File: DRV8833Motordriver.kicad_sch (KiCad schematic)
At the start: 8 parts, among them J1 Conn_01x06_Pin, J2 Conn_01x06_Pin, U1 DRV8833PWP

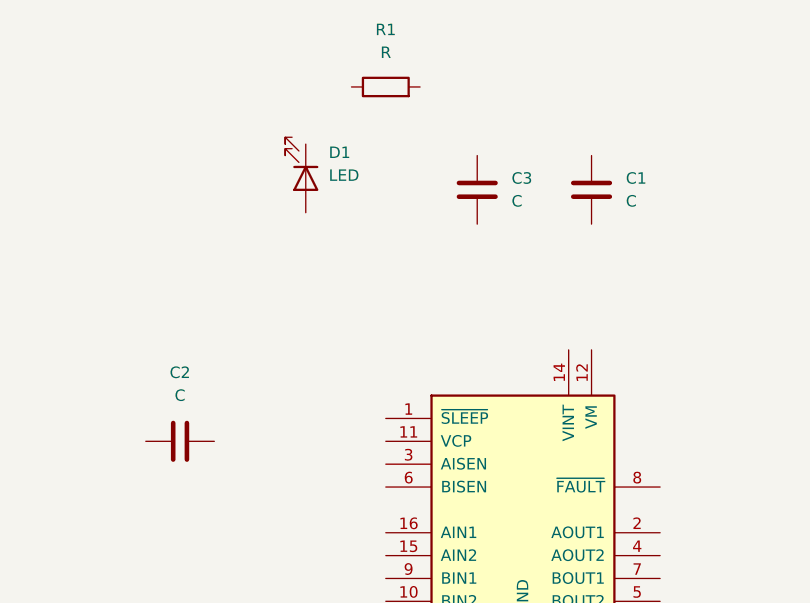
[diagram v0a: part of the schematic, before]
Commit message: Placed Normal Wires
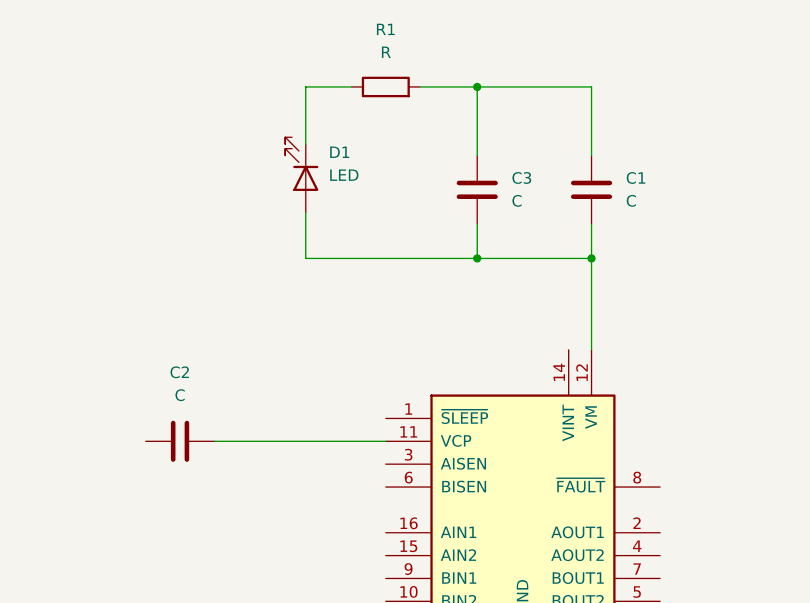
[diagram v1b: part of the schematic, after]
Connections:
- net at R1.1: now also D1.1 (K)
- net at R1.2: now also C1.1, C3.1
- net at C3.2: now also C1.2, D1.2 (A), U1.12 (VM)
- net at C2.2: now also U1.11 (VCP)
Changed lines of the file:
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@@
 	(generator_version "9.0")
 	(paper "A4")
+	(junction
+		(at 151.13 69.85)
+		(diameter 0)
+		(color 0 0 0 0)
+	)
+	(junction
+		(at 138.43 69.85)
+		(diameter 0)
+		(color 0 0 0 0)
+	)
+	(junction
+		(at 138.43 50.8)
+		(diameter 0)
+		(color 0 0 0 0)
+	)
+	(wire
+		(pts
+			(xy 119.38 50.8) (xy 124.46 50.8)
+		)
+		(stroke
+			(width 0)
+			(type default)
+		)
+	)
+	(wire
+		(pts
+			(xy 119.38 64.77) (xy 119.38 69.85)
+		)
+		(stroke
+			(width 0)
+			(type default)
+		)
+	)
+	(wire
+		(pts
+			(xy 138.43 69.85) (xy 151.13 69.85)
+		)
+		(stroke
+			(width 0)
+			(type default)
+		)
+	)
+	(wire
+		(pts
+			(xy 151.13 69.85) (xy 151.13 80.01)
+		)
+		(stroke
+			(width 0)
+			(type default)
+		)
+	)
+	(wire
+		(pts
+			(xy 138.43 66.04) (xy 138.43 69.85)
+		)
+		(stroke
+			(width 0)
+			(type default)
+		)
+	)
+	(wire
+		(pts
+			(xy 119.38 69.85) (xy 138.43 69.85)
+		)
+		(stroke
+			(width 0)
+			(type default)
+		)
+	)
+	(wire
+		(pts
+			(xy 138.43 50.8) (xy 132.08 50.8)
+		)
+		(stroke
+			(width 0)
+			(type default)
+		)
+	)
+	(wire
+		(pts
+			(xy 151.13 58.42) (xy 151.13 50.8)
+		)
+		(stroke
+			(width 0)
+			(type default)
+		)
+	)
+	(wire
+		(pts
+			(xy 151.13 66.04) (xy 151.13 69.85)
+		)
+		(stroke
+			(width 0)
+			(type default)
+		)
+	)
+	(wire
+		(pts
+			(xy 138.43 50.8) (xy 138.43 58.42)
+		)
+		(stroke
+			(width 0)
+			(type default)
+		)
+	)
+	(wire
+		(pts
+			(xy 109.22 90.17) (xy 128.27 90.17)
+		)
+		(stroke
+			(width 0)
+			(type default)
+		)
+	)
+	(wire
+		(pts
+			(xy 119.38 57.15) (xy 119.38 50.8)
+		)
+		(stroke
+			(width 0)
+			(type default)
+		)
+	)
+	(wire
+		(pts
+			(xy 151.13 50.8) (xy 138.43 50.8)
+		)
+		(stroke
+			(width 0)
+			(type default)
+		)
+	)
 	(symbol
 		(lib_id "Device:R")

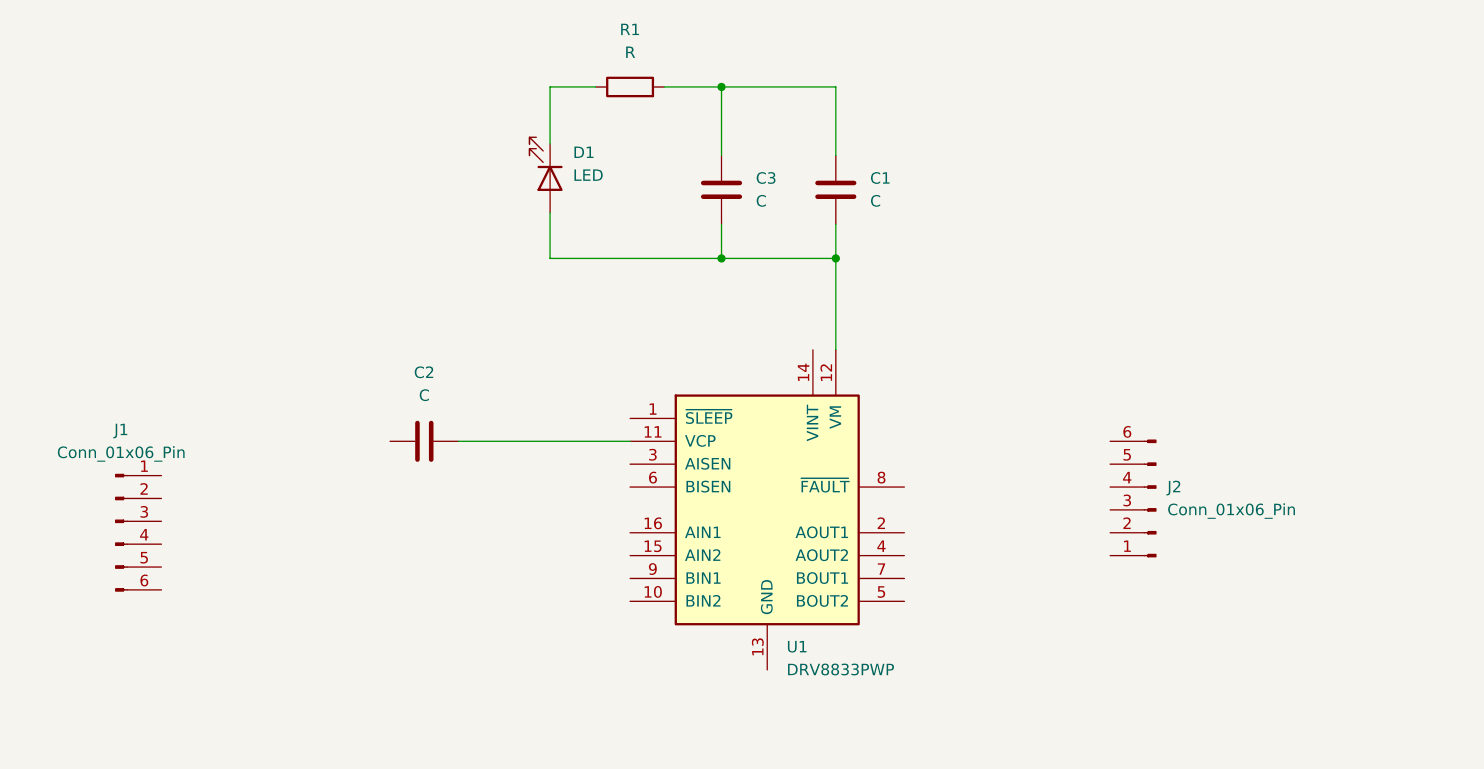
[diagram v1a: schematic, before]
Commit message: Added Net Labels to Wires
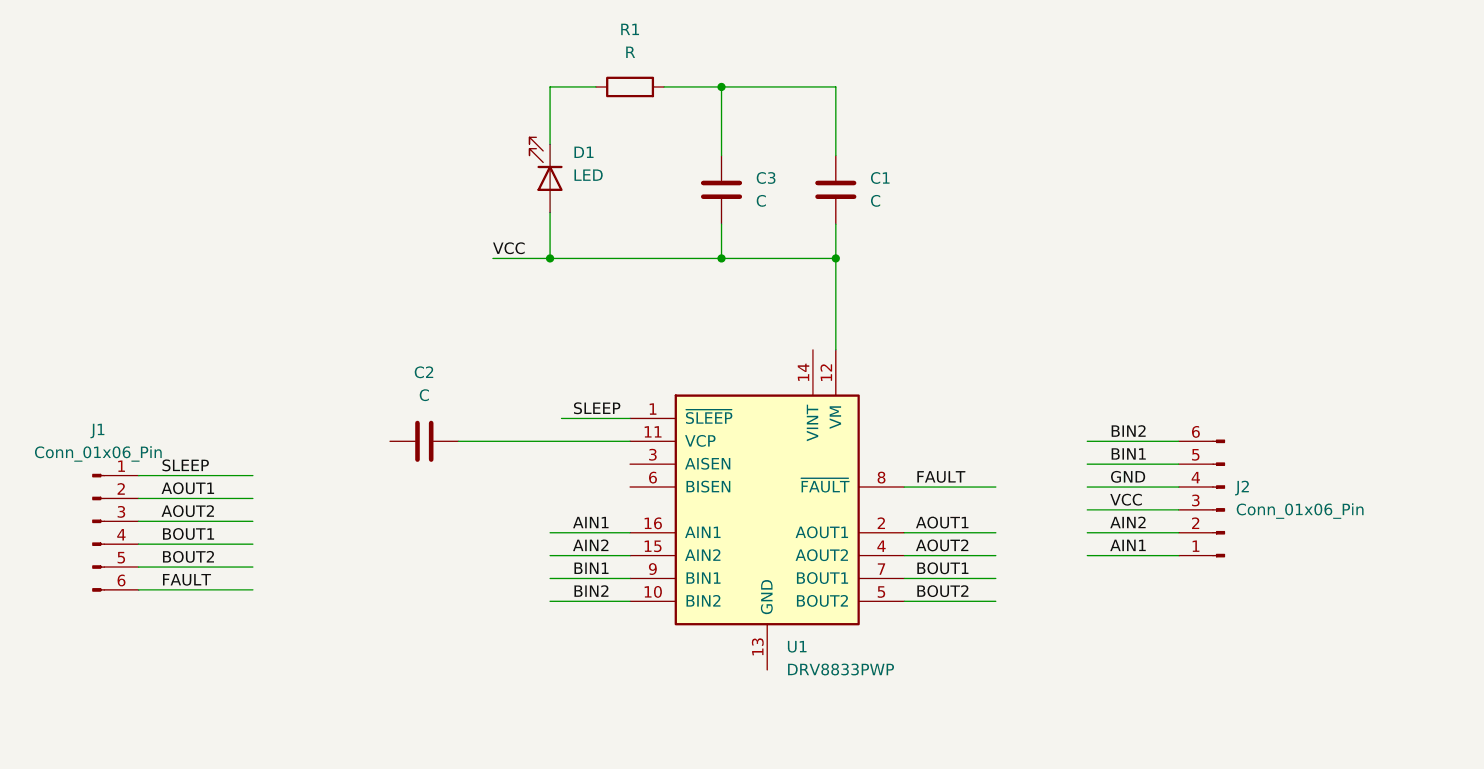
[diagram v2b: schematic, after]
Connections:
- net SLEEP: now reaches J1.1 (Pin_1)
- net SLEEP: now also U1.1 (~{SLEEP})
- net AOUT1: now reaches J1.2 (Pin_2)
- net AOUT1: now also U1.2 (AOUT1)
- net AOUT2: now reaches J1.3 (Pin_3)
- net AOUT2: now also U1.4 (AOUT2)
- net BOUT1: now reaches J1.4 (Pin_4)
- net BOUT1: now also U1.7 (BOUT1)
- net BOUT2: now reaches J1.5 (Pin_5)
- net BOUT2: now also U1.5 (BOUT2)
- net FAULT: now reaches J1.6 (Pin_6)
- net FAULT: now also U1.8 (~{FAULT})
- net VCC: now reaches C1.2, C3.2, D1.2 (A), U1.12 (VM)
- net VCC: now also J2.3 (Pin_3)
- net BIN2: now reaches U1.10 (BIN2)
- net BIN2: now also J2.6 (Pin_6)
- net AIN2: now reaches U1.15 (AIN2)
- net AIN2: now also J2.2 (Pin_2)
- net AIN1: now reaches U1.16 (AIN1)
- net AIN1: now also J2.1 (Pin_1)
- net BIN1: now reaches U1.9 (BIN1)
- net BIN1: now also J2.5 (Pin_5)
- net GND: now reaches J2.4 (Pin_4)
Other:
- moved on the sheet: J1, J2

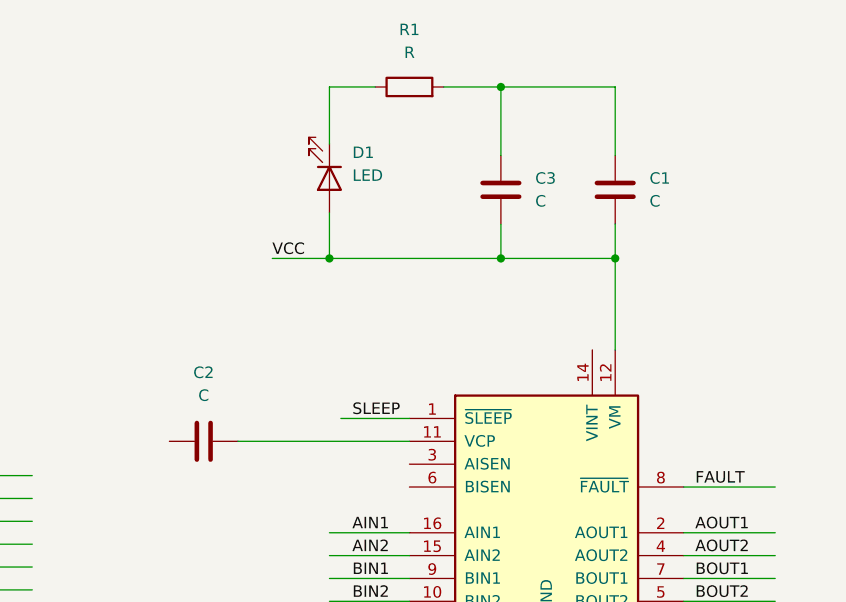
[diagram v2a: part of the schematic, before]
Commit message: Added Values to Components
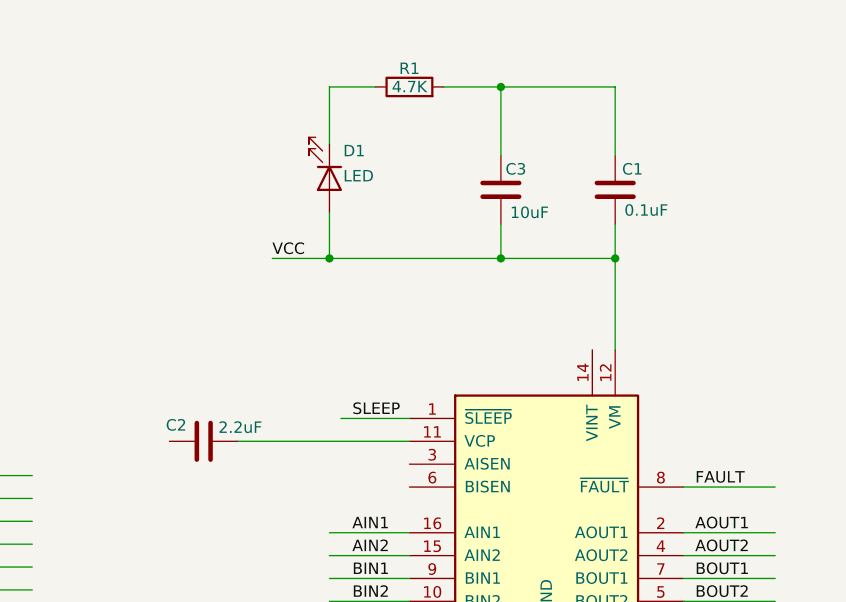
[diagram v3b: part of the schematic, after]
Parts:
- C1: value C -> 0.1uF
- C2: value C -> 2.2uF
- C3: value C -> 10uF
- R1: value R -> 4.7K
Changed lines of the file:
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@@
 		(on_board yes)
 		(dnp no)
-		(fields_autoplaced yes)
 		(property "Reference" "R1"
-			(at 128.27 44.45 90)
-			(effects
-				(font
-					(size 1.27 1.27)
-				)
-			)
-		)
-		(property "Value" "R"
-			(at 128.27 46.99 90)
+			(at 128.27 48.768 90)
+			(effects
+				(font
+					(size 1.27 1.27)
+				)
+			)
+		)
+		(property "Value" "4.7K"
+			(at 128.27 50.8 90)
 			(effects
 				(font
@@
 		(on_board yes)
 		(dnp no)
-		(fields_autoplaced yes)
 		(property "Reference" "C3"
-			(at 142.24 60.9599 0)
-			(effects
-				(font
-					(size 1.27 1.27)
-				)
-				(justify left)
-			)
-		)
-		(property "Value" "C"
-			(at 142.24 63.4999 0)
+			(at 138.938 59.944 0)
+			(effects
+				(font
+					(size 1.27 1.27)
+				)
+				(justify left)
+			)
+		)
+		(property "Value" "10uF"
+			(at 139.446 64.77 0)
 			(effects
 				(font
@@
 		(on_board yes)
 		(dnp no)
-		(fields_autoplaced yes)
 		(property "Reference" "C2"
-			(at 105.41 82.55 90)
-			(effects
-				(font
-					(size 1.27 1.27)
-				)
-			)
-		)
-		(property "Value" "C"
-			(at 105.41 85.09 90)
+			(at 102.362 88.392 90)
+			(effects
+				(font
+					(size 1.27 1.27)
+				)
+			)
+		)
+		(property "Value" "2.2uF"
+			(at 109.474 88.646 90)
 			(effects
 				(font
@@
 		(on_board yes)
 		(dnp no)
-		(fields_autoplaced yes)
 		(property "Reference" "D1"
-			(at 121.92 58.1024 90)
+			(at 120.904 57.912 90)
 			(effects
 				(font
@@
 		)
 		(property "Value" "LED"
-			(at 121.92 60.6424 90)
+			(at 120.904 60.706 90)
 			(effects
 				(font
@@
 		(on_board yes)
 		(dnp no)
-		(fields_autoplaced yes)
 		(property "Reference" "C1"
-			(at 154.94 60.9599 0)
-			(effects
-				(font
-					(size 1.27 1.27)
-				)
-				(justify left)
-			)
-		)
-		(property "Value" "C"
-			(at 154.94 63.4999 0)
-			(effects
-				(font
+			(at 151.892 59.944 0)
+			(effects
+				(font
+					(size 1.27 1.27)
+				)
+				(justify left)
+			)
+		)
+		(property "Value" "0.1uF"
+			(at 152.146 64.516 0)
+			(effects
+				(font

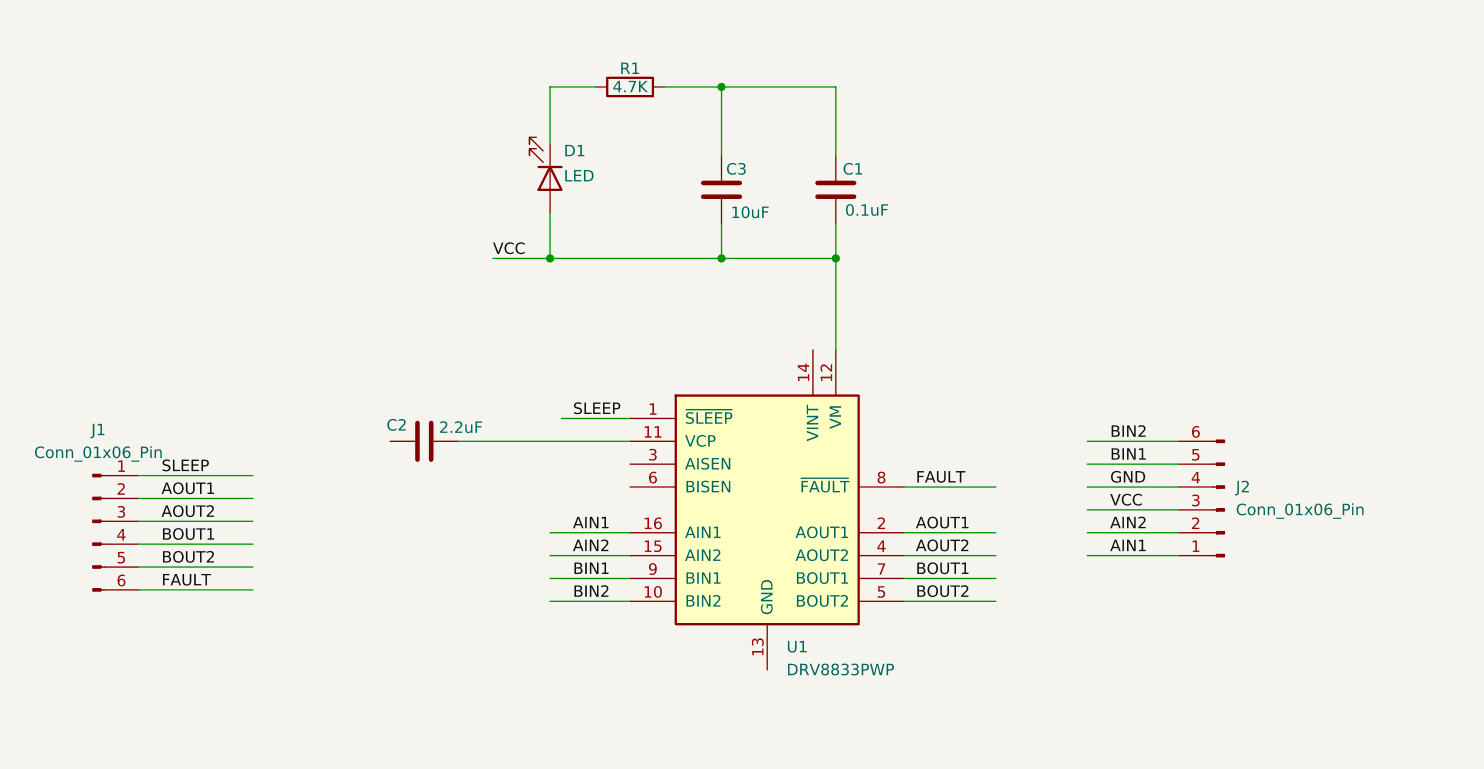
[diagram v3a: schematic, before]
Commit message: Added GND and PWR flag
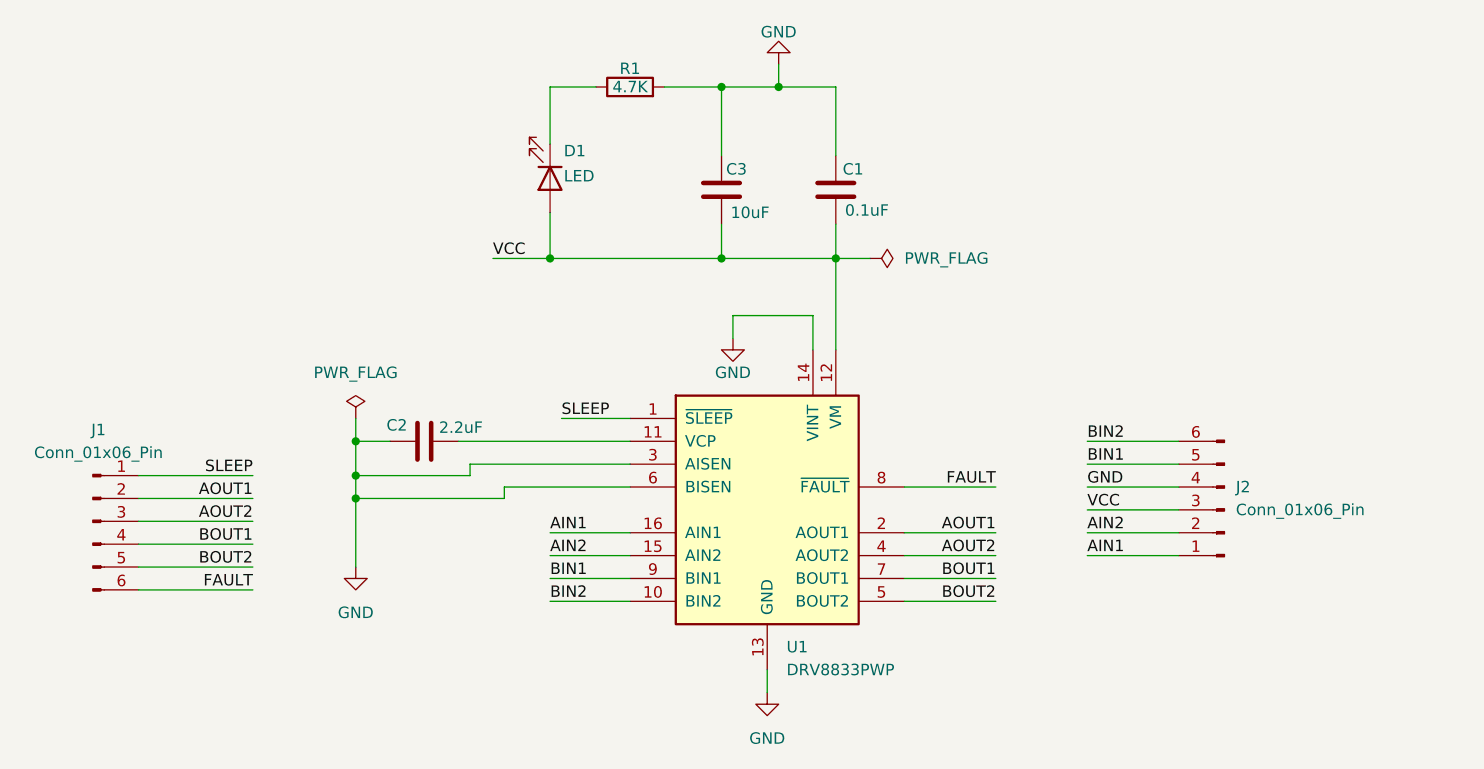
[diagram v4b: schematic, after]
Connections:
- net GND: now also C1.1, C2.1, C3.1, R1.2, U1.13 (GND), U1.14 (VINT), U1.17 (GND), U1.3 (AISEN), U1.6 (BISEN)

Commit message: Assigned Footprints to Schematic Components
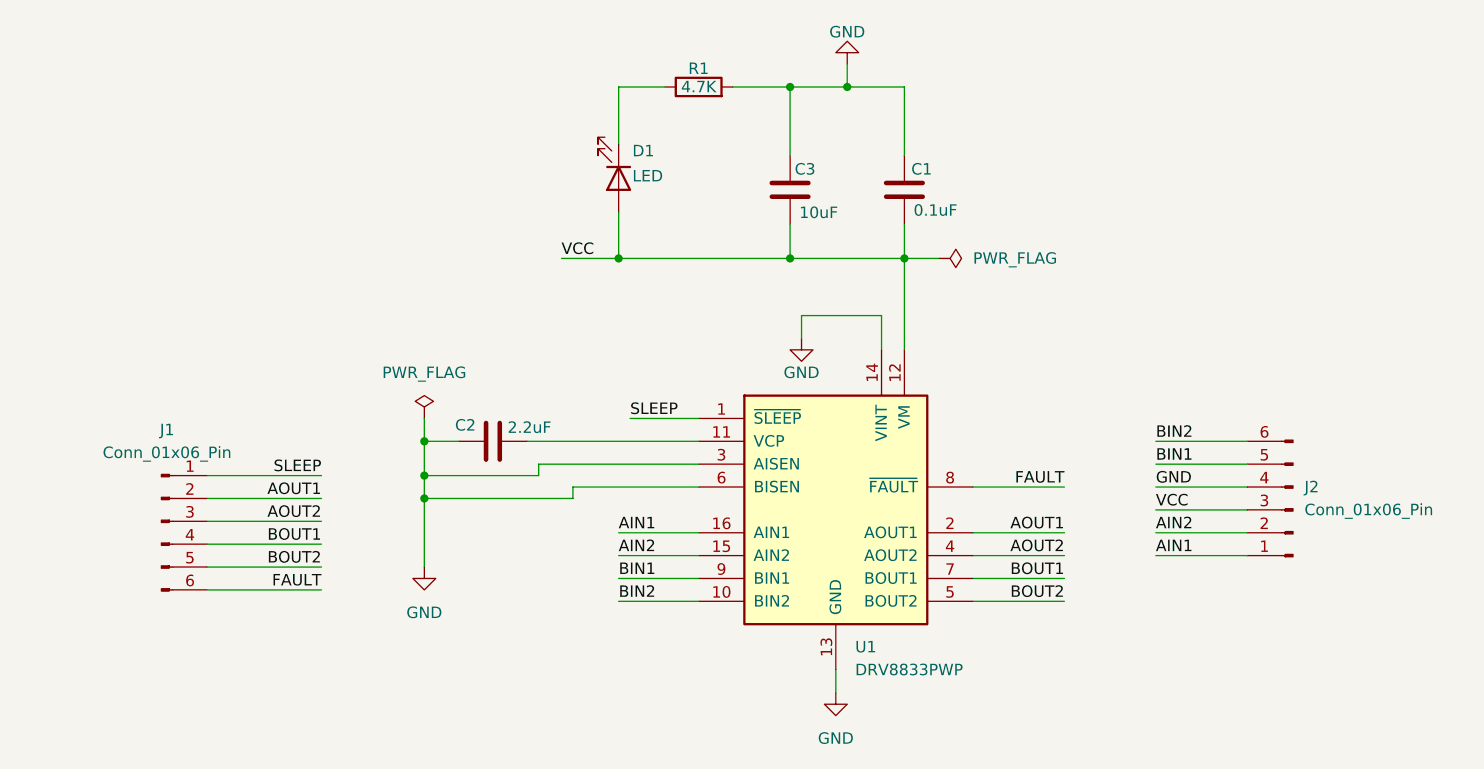
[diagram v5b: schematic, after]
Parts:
- C1, C2: footprint (none) -> Capacitor_SMD:C_0805_2012Metric
- C3: footprint (none) -> Capacitor_Tantalum_SMD:CP_EIA-6032-20_AVX-F
- D1: footprint (none) -> LED_SMD:LED_0805_2012Metric
- J1, J2: footprint (none) -> Connector_PinHeader_2.54mm:PinHeader_1x06_P2.54mm_Vertical
- R1: footprint (none) -> Resistor_SMD:R_0805_2012Metric
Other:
- moved on the sheet: C1, C2, C3, D1, J1, J2, R1, U1
